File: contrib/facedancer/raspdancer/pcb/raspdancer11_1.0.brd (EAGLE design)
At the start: 25.8 x 33.3 mm, 15 parts, among them Q1 12Mhz

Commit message: raspdancer pcb edited
thanks to Zac Franken for his tuning tips

git-svn-id: https://svn.code.sf.net/p/goodfet/code@1589 12e2690d-a6be-4b82-a7b7-67c4a43b65c8
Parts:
- removed C5: 1uF, 00_mylib:C1206
- J_RASP: device con-lsta:FE13-2 -> doegox:FE13-2
- moved C1 13.7 mm to (16.9, 8.64), turned to 0 degrees
- moved Q1 7.88 mm to (16.4, 29.5), turned to 90 degrees
- moved C2 4.13 mm to (16.8, 22.9)
- moved C3 3.19 mm to (11.0, 30.6), turned to 180 degrees
- moved C4 1.11 mm to (4.00, 30.6), turned to 180 degrees
- moved JP2 0.32 mm to (16.8, 16.5)
- moved JP4 0.32 mm to (16.8, 12.7)
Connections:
- net GND: no longer C5.1
- net VBUS: now also C1.2; no longer C5.2
- net VCC: no longer C1.2
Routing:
- net VBUS: track 50.0 -> 58.6 mm
- net XO: track 10.7 -> 17.4 mm
- net IX: track 10.4 -> 12.2 mm
- net RES: track 21.1 -> 19.8 mm
- net D+2: track 6.35 -> 7.11 mm
- net VCC: track 25.3 -> 25.8 mm, vias 0 -> 1
- net VBUS2: track 10.2 -> 9.67 mm
- net INT: track 6.77 -> 6.27 mm
- net INT2: track 10.2 -> 10.5 mm, vias 0 -> 1
- net GPX2: track 10.5 -> 10.8 mm, vias 0 -> 1
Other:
- board text added: "Raspdancer11 V1.0 by JCN & doegox"
- board text removed: "Raspdancer11 V1.0 JCN & doegox design"

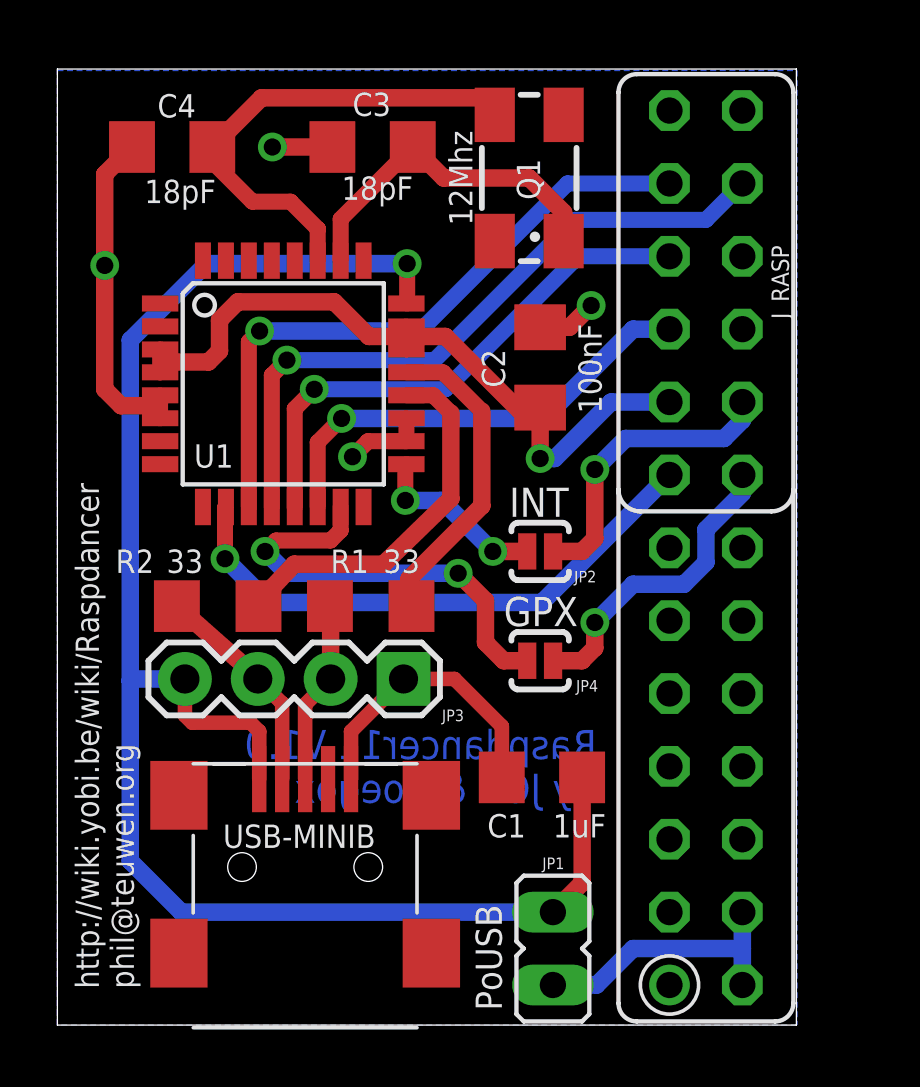
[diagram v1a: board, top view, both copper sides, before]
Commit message: raspdancer21: fix silkscreen
git-svn-id: https://svn.code.sf.net/p/goodfet/code@1590 12e2690d-a6be-4b82-a7b7-67c4a43b65c8
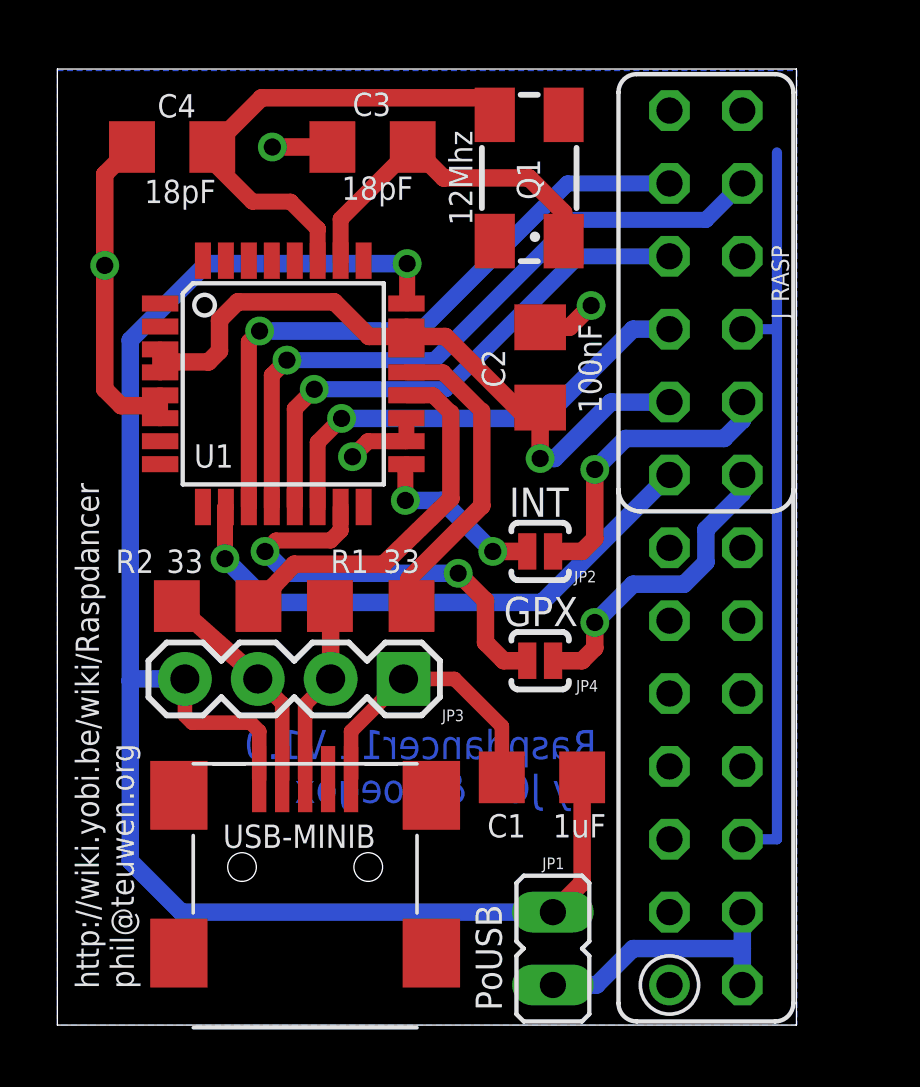
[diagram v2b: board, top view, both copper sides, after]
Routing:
- net GND: track 29.7 -> 56.1 mm
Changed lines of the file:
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@@
 <layer number="27" name="tValues" color="7" fill="1" visible="yes" active="yes"/>
 <layer number="28" name="bValues" color="7" fill="1" visible="yes" active="yes"/>
-<layer number="29" name="tStop" color="7" fill="3" visible="yes" active="yes"/>
-<layer number="30" name="bStop" color="7" fill="6" visible="yes" active="yes"/>
-<layer number="31" name="tCream" color="7" fill="4" visible="yes" active="yes"/>
-<layer number="32" name="bCream" color="7" fill="5" visible="yes" active="yes"/>
-<layer number="33" name="tFinish" color="6" fill="3" visible="yes" active="yes"/>
-<layer number="34" name="bFinish" color="6" fill="6" visible="yes" active="yes"/>
-<layer number="35" name="tGlue" color="7" fill="4" visible="yes" active="yes"/>
-<layer number="36" name="bGlue" color="7" fill="5" visible="yes" active="yes"/>
-<layer number="37" name="tTest" color="7" fill="1" visible="yes" active="yes"/>
-<layer number="38" name="bTest" color="7" fill="1" visible="yes" active="yes"/>
-<layer number="39" name="tKeepout" color="4" fill="11" visible="yes" active="yes"/>
-<layer number="40" name="bKeepout" color="1" fill="11" visible="yes" active="yes"/>
-<layer number="41" name="tRestrict" color="4" fill="10" visible="yes" active="yes"/>
-<layer number="42" name="bRestrict" color="1" fill="10" visible="yes" active="yes"/>
-<layer number="43" name="vRestrict" color="2" fill="10" visible="yes" active="yes"/>
-<layer number="44" name="Drills" color="7" fill="1" visible="yes" active="yes"/>
-<layer number="45" name="Holes" color="7" fill="1" visible="yes" active="yes"/>
-<layer number="46" name="Milling" color="3" fill="1" visible="yes" active="yes"/>
-<layer number="47" name="Measures" color="7" fill="1" visible="yes" active="yes"/>
-<layer number="48" name="Document" color="7" fill="1" visible="yes" active="yes"/>
-<layer number="49" name="Reference" color="7" fill="1" visible="yes" active="yes"/>
-<layer number="50" name="dxf" color="7" fill="1" visible="yes" active="yes"/>
+<layer number="29" name="tStop" color="7" fill="3" visible="no" active="yes"/>
+<layer number="30" name="bStop" color="7" fill="6" visible="no" active="yes"/>
+<layer number="31" name="tCream" color="7" fill="4" visible="no" active="yes"/>
+<layer number="32" name="bCream" color="7" fill="5" visible="no" active="yes"/>
+<layer number="33" name="tFinish" color="6" fill="3" visible="no" active="yes"/>
+<layer number="34" name="bFinish" color="6" fill="6" visible="no" active="yes"/>
+<layer number="35" name="tGlue" color="7" fill="4" visible="no" active="yes"/>
+<layer number="36" name="bGlue" color="7" fill="5" visible="no" active="yes"/>
+<layer number="37" name="tTest" color="7" fill="1" visible="no" active="yes"/>
+<layer number="38" name="bTest" color="7" fill="1" visible="no" active="yes"/>
+<layer number="39" name="tKeepout" color="4" fill="11" visible="no" active="yes"/>
+<layer number="40" name="bKeepout" color="1" fill="11" visible="no" active="yes"/>
+<layer number="41" name="tRestrict" color="4" fill="10" visible="no" active="yes"/>
+<layer number="42" name="bRestrict" color="1" fill="10" visible="no" active="yes"/>
+<layer number="43" name="vRestrict" color="2" fill="10" visible="no" active="yes"/>
+<layer number="44" name="Drills" color="7" fill="1" visible="no" active="yes"/>
+<layer number="45" name="Holes" color="7" fill="1" visible="no" active="yes"/>
+<layer number="46" name="Milling" color="3" fill="1" visible="no" active="yes"/>
+<layer number="47" name="Measures" color="7" fill="1" visible="no" active="yes"/>
+<layer number="48" name="Document" color="7" fill="1" visible="no" active="yes"/>
+<layer number="49" name="Reference" color="7" fill="1" visible="no" active="yes"/>
+<layer number="50" name="dxf" color="7" fill="1" visible="no" active="yes"/>
 <layer number="51" name="tDocu" color="7" fill="1" visible="yes" active="yes"/>
 <layer number="52" name="bDocu" color="7" fill="1" visible="yes" active="yes"/>
 <layer number="53" name="tGND_GNDA" color="7" fill="9" visible="no" active="no"/>
 <layer number="54" name="bGND_GNDA" color="1" fill="9" visible="no" active="no"/>
-<layer number="56" name="wert" color="7" fill="1" visible="yes" active="yes"/>
+<layer number="56" name="wert" color="7" fill="1" visible="no" active="yes"/>
 <layer number="91" name="Nets" color="2" fill="1" visible="no" active="no"/>
 <layer number="92" name="Busses" color="1" fill="1" visible="no" active="no"/>
@@
 <layer number="98" name="Guide" color="6" fill="1" visible="no" active="no"/>
 <layer number="100" name="Muster" color="7" fill="1" visible="no" active="no"/>
-<layer number="101" name="Patch_Top" color="12" fill="4" visible="yes" active="yes"/>
-<layer number="102" name="Vscore" color="7" fill="1" visible="yes" active="yes"/>
-<layer number="103" name="tMap" color="7" fill="1" visible="yes" active="yes"/>
-<layer number="104" name="Name" color="16" fill="1" visible="yes" active="yes"/>
-<layer number="105" name="tPlate" color="7" fill="1" visible="yes" active="yes"/>
-<layer number="106" name="bPlate" color="7" fill="1" visible="yes" active="yes"/>
-<layer number="107" name="Crop" color="7" fill="1" visible="yes" active="yes"/>
-<layer number="108" name="fp8" color="7" fill="1" visible="yes" active="yes"/>
-<layer number="109" name="fp9" color="7" fill="1" visible="yes" active="yes"/>
-<layer number="110" name="fp0" color="7" fill="1" visible="yes" active="yes"/>
-<layer number="111" name="LPC17xx" color="7" fill="1" visible="yes" active="yes"/>
+<layer number="101" name="Patch_Top" color="12" fill="4" visible="no" active="yes"/>
+<layer number="102" name="Vscore" color="7" fill="1" visible="no" active="yes"/>
+<layer number="103" name="tMap" color="7" fill="1" visible="no" active="yes"/>
+<layer number="104" name="Name" color="16" fill="1" visible="no" active="yes"/>
+<layer number="105" name="tPlate" color="7" fill="1" visible="no" active="yes"/>
+<layer number="106" name="bPlate" color="7" fill="1" visible="no" active="yes"/>
+<layer number="107" name="Crop" color="7" fill="1" visible="no" active="yes"/>
+<layer number="108" name="fp8" color="7" fill="1" visible="no" active="yes"/>
+<layer number="109" name="fp9" color="7" fill="1" visible="no" active="yes"/>
+<layer number="110" name="fp0" color="7" fill="1" visible="no" active="yes"/>
+<layer number="111" name="LPC17xx" color="7" fill="1" visible="no" active="yes"/>
 <layer number="112" name="tSilk" color="7" fill="1" visible="no" active="yes"/>
 <layer number="116" name="Patch_BOT" color="9" fill="4" visible="no" active="yes"/>
@@
 <wire x1="15.494" y1="10.414" x2="15.494" y2="8.639" width="0.508" layer="1"/>
 <wire x1="15.494" y1="8.639" x2="15.491" y2="8.636" width="0.508" layer="1"/>
+<wire x1="23.876" y1="24.257" x2="25.0825" y2="24.257" width="0.3556" layer="16"/>
+<wire x1="23.876" y1="6.477" x2="25.0825" y2="6.477" width="0.3556" layer="16"/>
+<wire x1="25.0825" y1="30.4165" x2="25.0825" y2="6.477" width="0.3556" layer="16"/>
 <wire x1="3.5814" y1="21.1836" x2="3.5814" y2="21.152" width="0" layer="19" extent="1-1"/>
+<wire x1="16.8275" y1="24.3235" x2="12.1666" y2="21.152" width="0" layer="19" extent="1-1"/>
 </signal>
 <signal name="VCC">

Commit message: raspdancer11/21 PCB: more room along connector & larger vias for raspdancer11
git-svn-id: https://svn.code.sf.net/p/goodfet/code@1591 12e2690d-a6be-4b82-a7b7-67c4a43b65c8
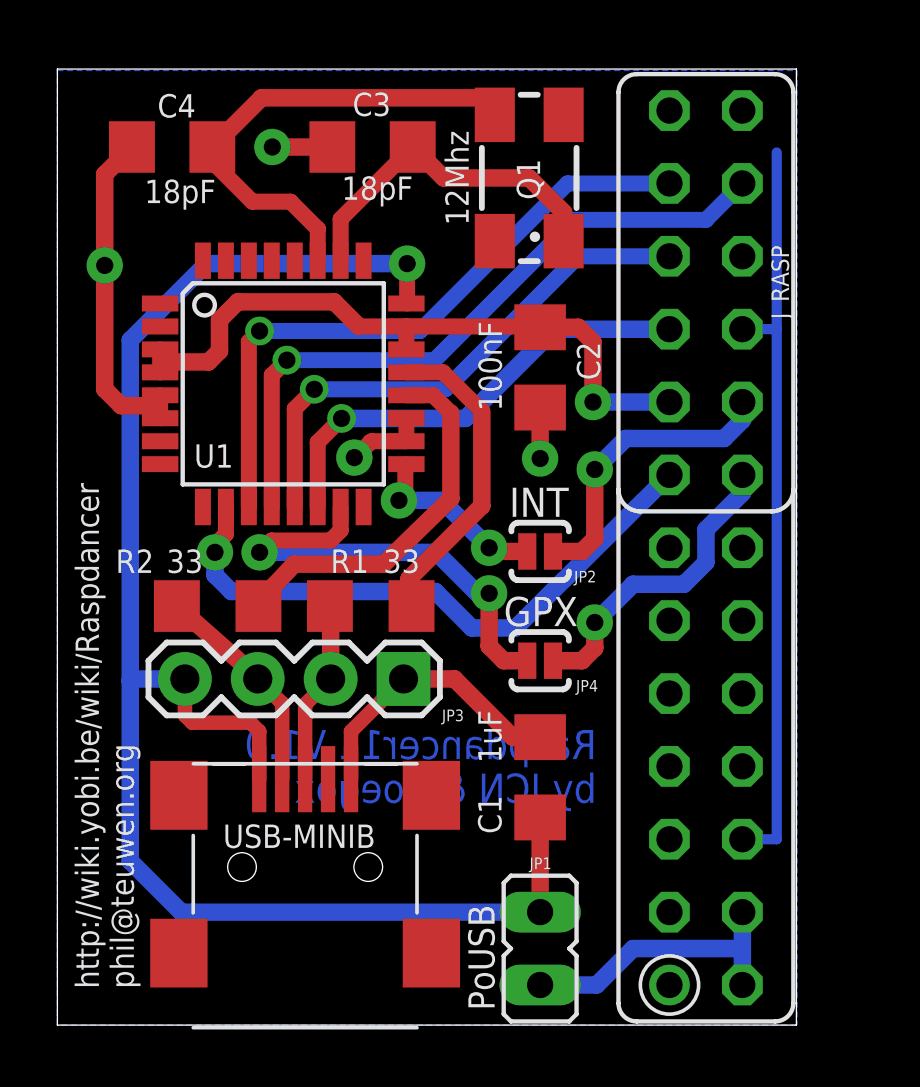
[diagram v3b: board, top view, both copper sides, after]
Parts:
- moved JP1 0.44 mm to (16.8, 2.67)
- moved C1 0.06 mm to (16.8, 8.64), turned to 270 degrees
- turned C2 to 90 degrees
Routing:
- net VBUS: track 58.6 -> 56.4 mm
- net VCC: track 25.8 -> 23.7 mm
- net GND: track 56.1 -> 57.8 mm
- net RES: track 19.8 -> 21.4 mm
- net GPX: track 15.3 -> 15.9 mm

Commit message: raspdancer: larger wires & vias & some tunings
git-svn-id: https://svn.code.sf.net/p/goodfet/code@1592 12e2690d-a6be-4b82-a7b7-67c4a43b65c8
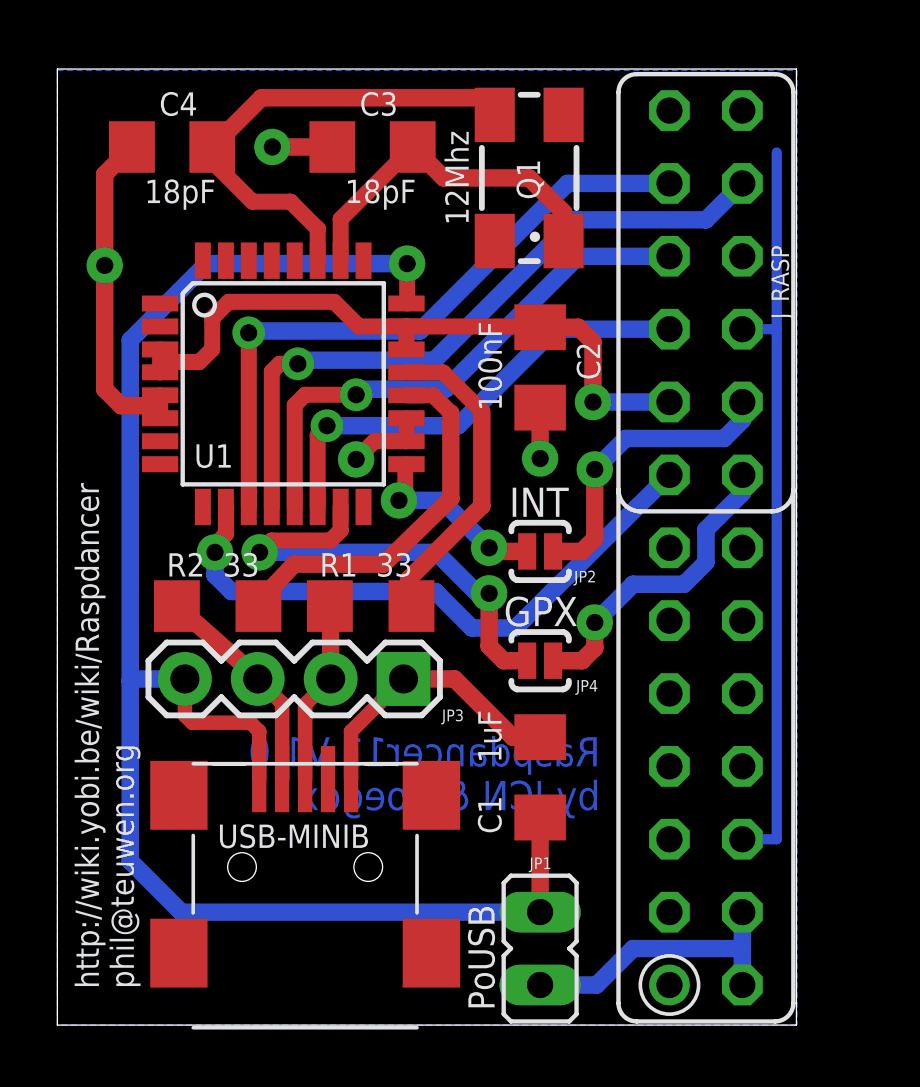
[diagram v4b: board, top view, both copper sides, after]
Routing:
- net GND: track 57.8 -> 55.7 mm
